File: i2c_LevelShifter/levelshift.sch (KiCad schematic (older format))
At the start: 6 parts, among them Q1 BSS138, Q2 BSS138

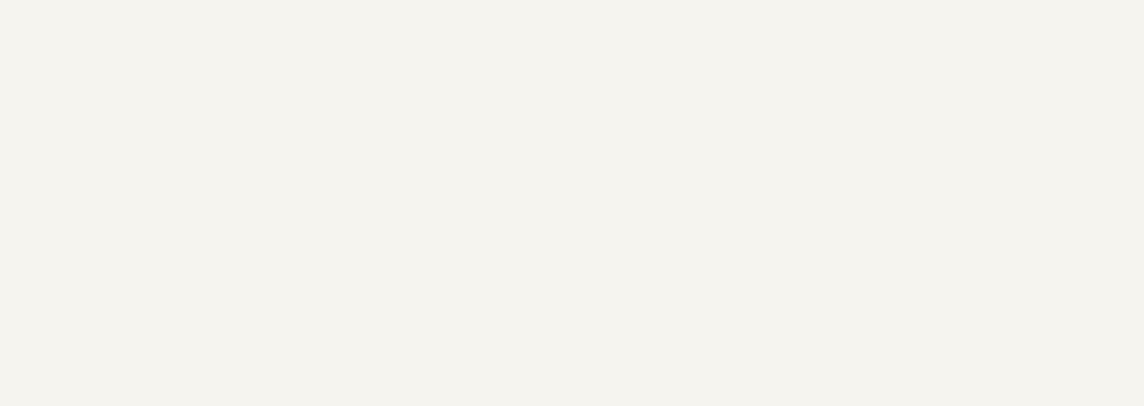
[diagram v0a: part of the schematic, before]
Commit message: added CreativeCommons License
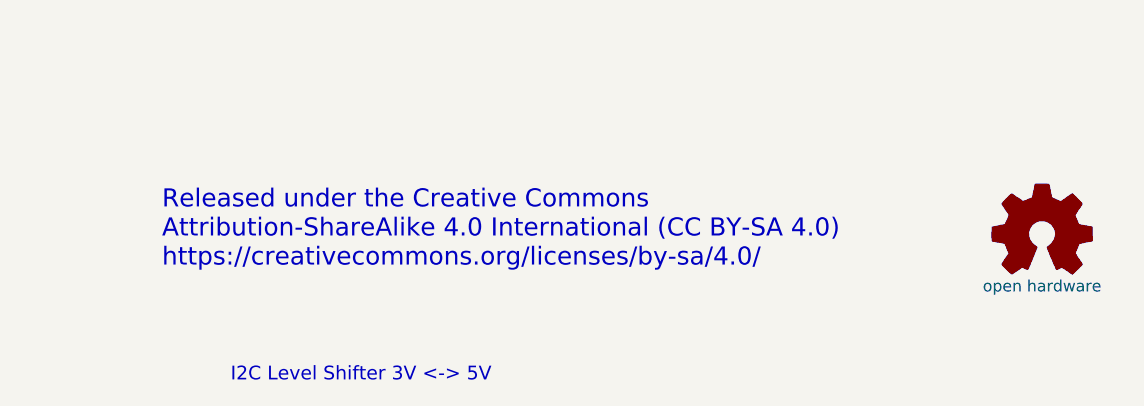
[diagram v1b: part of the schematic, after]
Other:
- note added: "I2C Level Shifter 3V <-> 5V"
- note added: "Released under the Creative Commons\nAttribution-ShareAlike 4.0 International (CC BY-SA 4.0) \nhttps://creativecommons.org/licenses/by-sa/4.0/"
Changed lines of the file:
@@
 LIBS:contrib
 LIBS:valves
+LIBS:graphic_symbols
+LIBS:levelshift-cache
 EELAYER 25 0
 EELAYER END
@@
 Text HLabel 3850 3750 0    60   Input ~ 0
 CLK_3V
+Text Notes 7350 7500 0    60   ~ 0
+I2C Level Shifter 3V <-> 5V
+Text Notes 7050 7000 0    79   ~ 0
+Released under the Creative Commons\nAttribution-ShareAlike 4.0 International (CC BY-SA 4.0) \nhttps://creativecommons.org/licenses/by-sa/4.0/
+$Comp
+L Logo_Open_Hardware_Small #LOGO?
+U 1 1 59A1F889
+P 10900 6850
+F 0 "#LOGO?" H 10900 7125 50  0001 C CNN
+F 1 "open hardware" H 10900 6625 50  0000 C CNN
+F 2 "" H 10900 6850 50  0001 C CNN
+F 3 "" H 10900 6850 50  0001 C CNN
+	1    10900 6850
+	1    0    0    -1
+$EndComp
 $EndSCHEMATC
